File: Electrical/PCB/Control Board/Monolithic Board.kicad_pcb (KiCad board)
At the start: 2 copper layers, 154 x 175 mm, 89 parts, among them J1 ED2627-ND, J10 6posheader, J11 S7038-ND, J12 ED2989-ND-USB, J13 ED1501-ND, J14 ED2989-ND-USB, J15 ED2580-ND, J16 ED2580-ND, J17 ED2744-ND, J18 ED2744-ND, J19 ED2744-ND, J2 ED2627-ND, J20 ED2744-ND, J21 ED2744-ND, J22 ED2744-ND, J23 ED2744-ND, J24 ED2744-ND, J25 ED2744-ND, J26 ED2744-ND, J3 ED2627-ND, J4 ED2627-ND, J5 ED2627-ND, J6 S9175-ND, J7 S9175-ND, J8 6posheader, J9 S7038-ND, M1 Mounting_Holes, T1 test_point, T10 test_point, T11 test_point, T12 test_point, T13 test_point, T14 test_point, T15 test_point, T16 test_point, T17 test_point, T18 test_point, T19 test_point, T2 test_point, T20 test_point, T21 test_point, T3 test_point, T4 test_point, T5 test_point, T6 test_point, T7 test_point, T8 test_point, T9 test_point, U1 LM358-N, U2 LM358-N

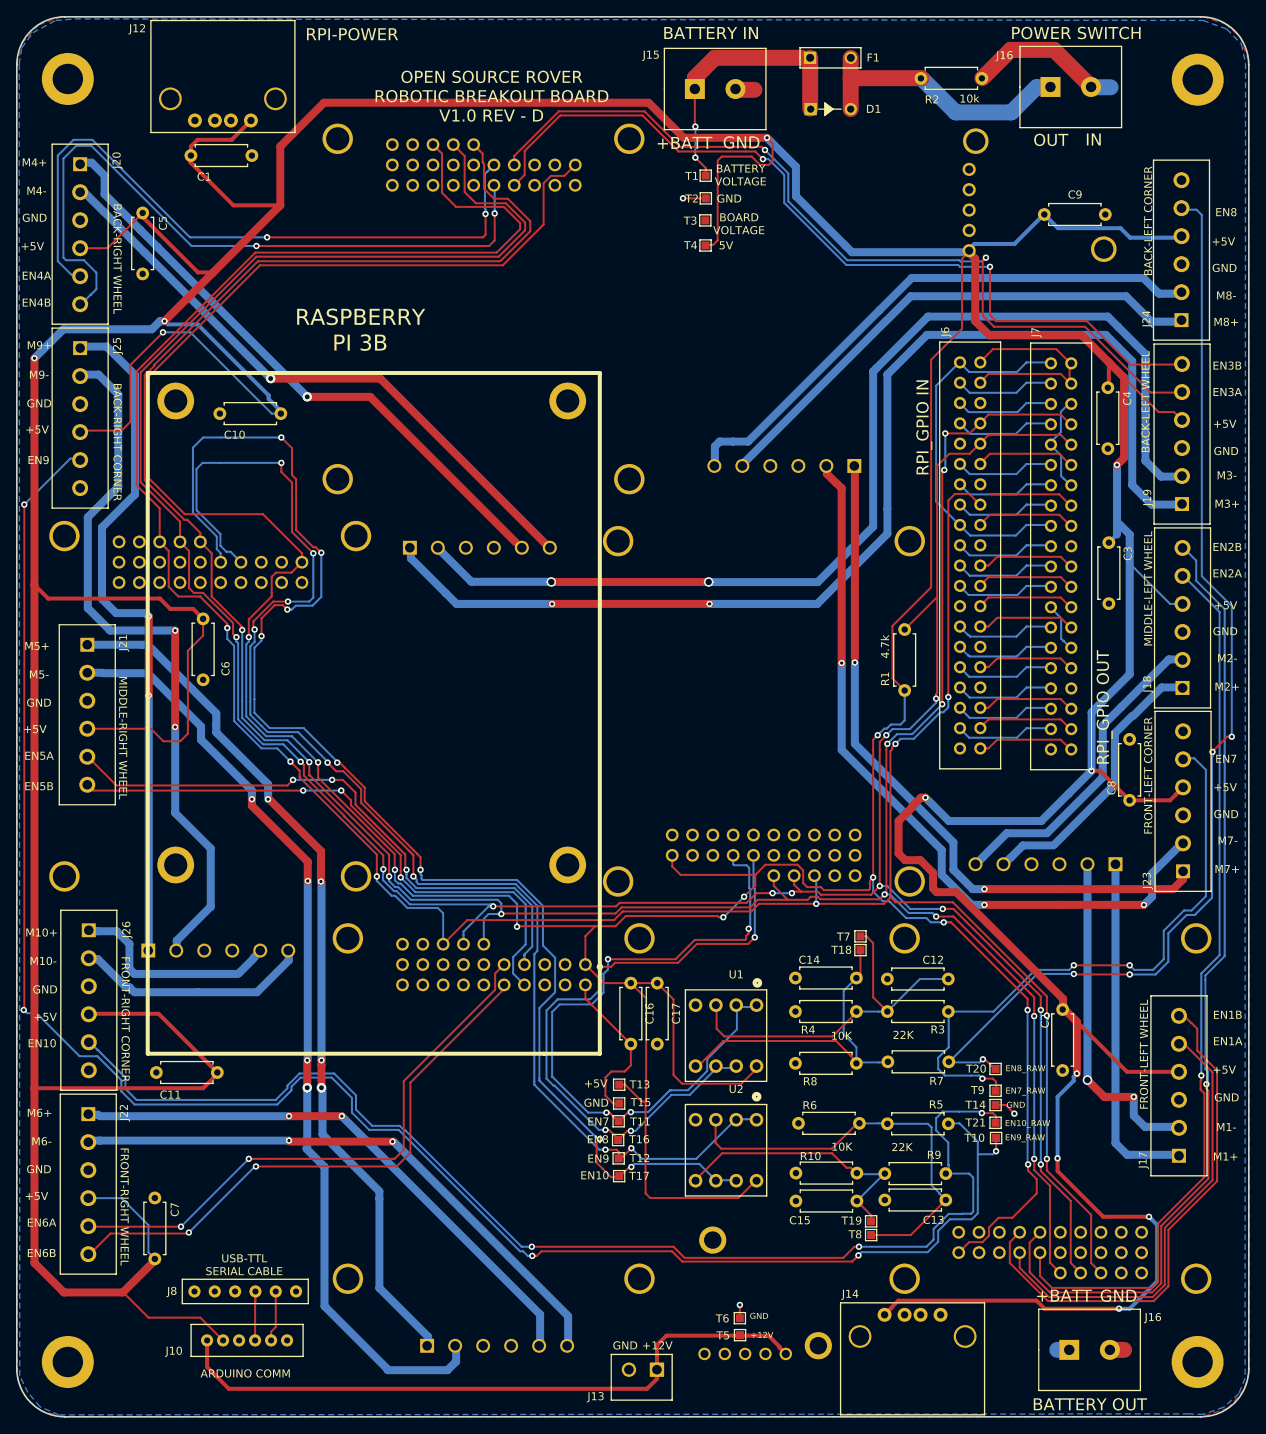
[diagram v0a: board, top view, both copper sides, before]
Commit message: Fixed silkscreen issues on Monolithic Board (Closes 119 and closes 123)
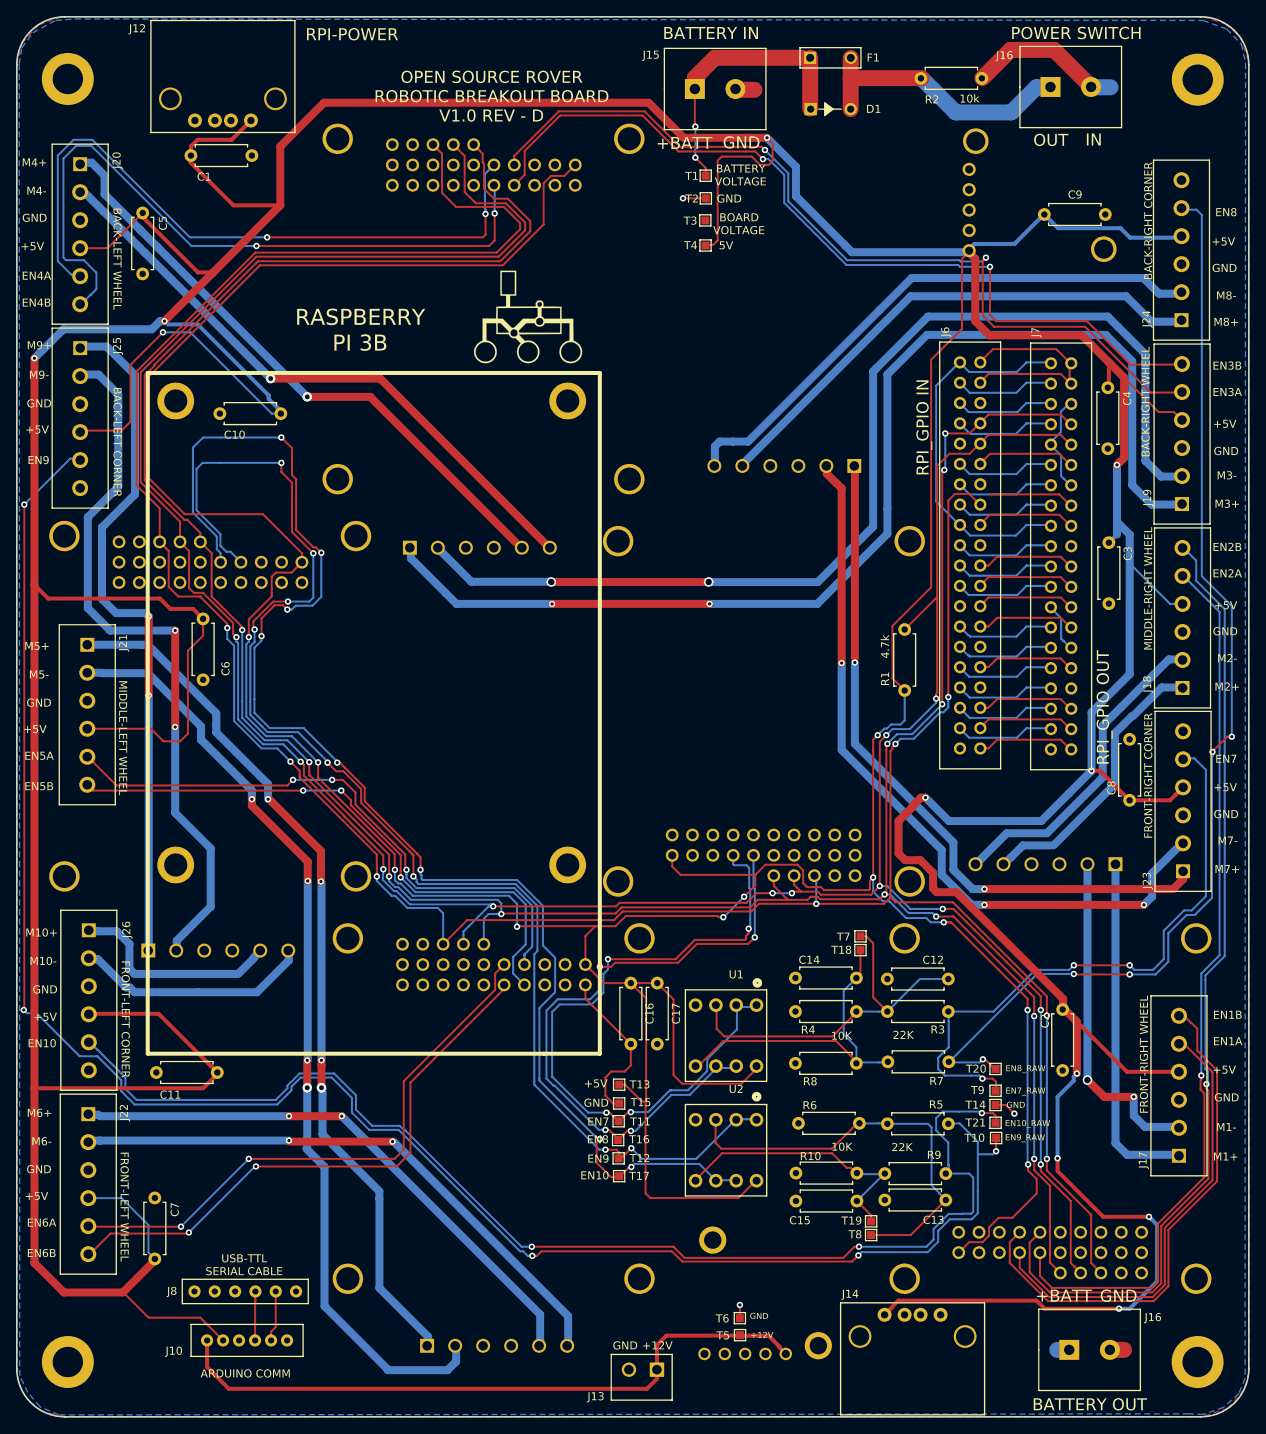
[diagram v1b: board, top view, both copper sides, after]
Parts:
- added G***: LOGO, JPL Robotics:rover_image, F.Cu at (63.4, -136.0)
